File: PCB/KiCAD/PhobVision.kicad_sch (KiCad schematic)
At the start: 9 parts

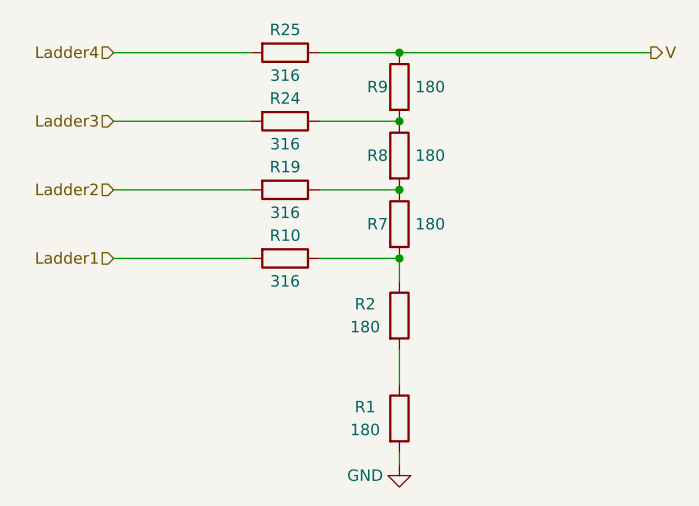
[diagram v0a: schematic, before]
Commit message: Assembly and fab upload
Upload schematic pdf and bom csv and ibom html docs
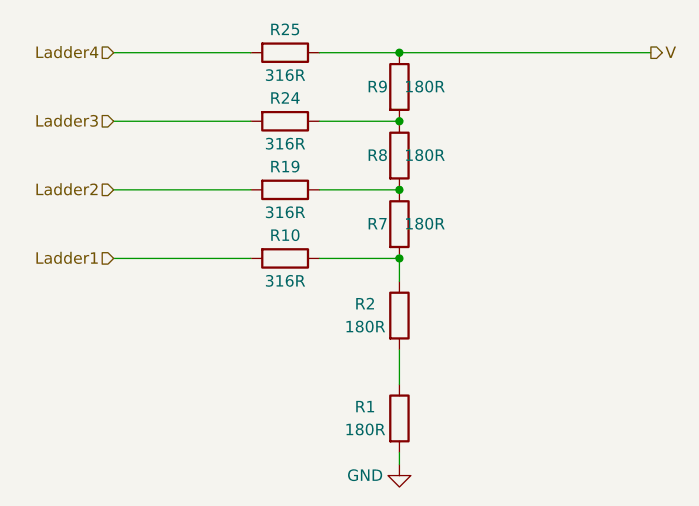
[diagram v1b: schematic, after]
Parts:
- R1, R2, R7, R8, R9: value 180 -> 180R; MPN (none) -> RC0402FR-07180RL; Manufacturer (none) -> YAGEO; Package (none) -> 0402; VARIANT (none) -> NoVar
- R10, R19, R24, R25: value 316 -> 316R; MPN (none) -> RC0402FR-07316RL; Manufacturer (none) -> YAGEO; Package (none) -> 0402; VARIANT (none) -> NoVar
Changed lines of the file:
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@@
       (effects (font (size 1.27 1.27)) (justify right))
     )
-    (property "Value" "180" (id 1) (at 144.78 87.63 0)
+    (property "Value" "180R" (id 1) (at 144.78 87.63 0)
       (effects (font (size 1.27 1.27)) (justify right))
     )
@@
     )
     (property "Datasheet" "~" (id 3) (at 139.7 87.63 0)
+      (effects (font (size 1.27 1.27)) hide)
+    )
+    (property "MPN" "RC0402FR-07180RL" (id 4) (at 139.7 87.63 0)
+      (effects (font (size 1.27 1.27)) hide)
+    )
+    (property "Manufacturer" "YAGEO" (id 5) (at 139.7 87.63 0)
+      (effects (font (size 1.27 1.27)) hide)
+    )
+    (property "Package" "0402" (id 6) (at 139.7 87.63 0)
+      (effects (font (size 1.27 1.27)) hide)
+    )
+    (property "VARIANT" "NoVar" (id 7) (at 139.7 87.63 0)
       (effects (font (size 1.27 1.27)) hide)
     )
@@
     (in_bom yes) (on_board yes)
     (property "Reference" "R19" (id 0) (at 127 88.9 90))
-    (property "Value" "316" (id 1) (at 127 93.98 90))
+    (property "Value" "316R" (id 1) (at 127 93.98 90))
     (property "Footprint" "PhobGCC_2_0_0_footprints:R_0402_1005Metric" (id 2) (at 127 89.662 90)
       (effects (font (size 1.27 1.27)) hide)
@@
       (effects (font (size 1.27 1.27)) hide)
     )
+    (property "MPN" "RC0402FR-07316RL" (id 4) (at 127 91.44 0)
+      (effects (font (size 1.27 1.27)) hide)
+    )
+    (property "Manufacturer" "YAGEO" (id 5) (at 127 91.44 0)
+      (effects (font (size 1.27 1.27)) hide)
+    )
+    (property "Package" "0402" (id 6) (at 127 91.44 0)
+      (effects (font (size 1.27 1.27)) hide)
+    )
+    (property "VARIANT" "NoVar" (id 7) (at 127 91.44 0)
+      (effects (font (size 1.27 1.27)) hide)
+    )
     (pin "1")
     (pin "2")
@@
     (in_bom yes) (on_board yes)
     (property "Reference" "R25" (id 0) (at 127 73.66 90))
-    (property "Value" "316" (id 1) (at 127 78.74 90))
+    (property "Value" "316R" (id 1) (at 127 78.74 90))
     (property "Footprint" "PhobGCC_2_0_0_footprints:R_0402_1005Metric" (id 2) (at 127 74.422 90)
       (effects (font (size 1.27 1.27)) hide)
@@
       (effects (font (size 1.27 1.27)) hide)
     )
+    (property "MPN" "RC0402FR-07316RL" (id 4) (at 127 76.2 0)
+      (effects (font (size 1.27 1.27)) hide)
+    )
+    (property "Manufacturer" "YAGEO" (id 5) (at 127 76.2 0)
+      (effects (font (size 1.27 1.27)) hide)
+    )
+    (property "Package" "0402" (id 6) (at 127 76.2 0)
+      (effects (font (size 1.27 1.27)) hide)
+    )
+    (property "VARIANT" "NoVar" (id 7) (at 127 76.2 0)
+      (effects (font (size 1.27 1.27)) hide)
+    )
     (pin "1")
     (pin "2")
@@
     (in_bom yes) (on_board yes)
     (property "Reference" "R10" (id 0) (at 127 96.52 90))
-    (property "Value" "316" (id 1) (at 127 101.6 90))
+    (property "Value" "316R" (id 1) (at 127 101.6 90))
     (property "Footprint" "PhobGCC_2_0_0_footprints:R_0402_1005Metric" (id 2) (at 127 97.282 90)
       (effects (font (size 1.27 1.27)) hide)
@@
       (effects (font (size 1.27 1.27)) hide)
     )
+    (property "MPN" "RC0402FR-07316RL" (id 4) (at 127 99.06 0)
+      (effects (font (size 1.27 1.27)) hide)
+    )
+    (property "Manufacturer" "YAGEO" (id 5) (at 127 99.06 0)
+      (effects (font (size 1.27 1.27)) hide)
+    )
+    (property "Package" "0402" (id 6) (at 127 99.06 0)
+      (effects (font (size 1.27 1.27)) hide)
+    )
+    (property "VARIANT" "NoVar" (id 7) (at 127 99.06 0)
+      (effects (font (size 1.27 1.27)) hide)
+    )
     (pin "1")
     (pin "2")
@@
       (effects (font (size 1.27 1.27)) (justify right))
     )
-    (property "Value" "180" (id 1) (at 144.78 95.25 0)
+    (property "Value" "180R" (id 1) (at 144.78 95.25 0)
       (effects (font (size 1.27 1.27)) (justify right))
     )
@@
       (effects (font (size 1.27 1.27)) hide)
     )
+    (property "MPN" "RC0402FR-07180RL" (id 4) (at 139.7 95.25 0)
+      (effects (font (size 1.27 1.27)) hide)
+    )
+    (property "Manufacturer" "YAGEO" (id 5) (at 139.7 95.25 0)
+      (effects (font (size 1.27 1.27)) hide)
+    )
+    (property "Package" "0402" (id 6) (at 139.7 95.25 0)
+      (effects (font (size 1.27 1.27)) hide)
+    )
+    (property "VARIANT" "NoVar" (id 7) (at 139.7 95.25 0)
+      (effects (font (size 1.27 1.27)) hide)
+    )
     (pin "1")
     (pin "2")
@@
     (in_bom yes) (on_board yes)
     (property "Reference" "R2" (id 0) (at 135.89 104.14 0))
-    (property "Value" "180" (id 1) (at 135.89 106.68 0))
+    (property "Value" "180R" (id 1) (at 135.89 106.68 0))
     (property "Footprint" "PhobGCC_2_0_0_footprints:R_0402_1005Metric" (id 2) (at 137.922 105.41 90)
       (effects (font (size 1.27 1.27)) hide)
@@
       (effects (font (size 1.27 1.27)) hide)
     )
+    (property "MPN" "RC0402FR-07180RL" (id 4) (at 139.7 105.41 0)
+      (effects (font (size 1.27 1.27)) hide)
+    )
+    (property "Manufacturer" "YAGEO" (id 5) (at 139.7 105.41 0)
+      (effects (font (size 1.27 1.27)) hide)
+    )
+    (property "Package" "0402" (id 6) (at 139.7 105.41 0)
+      (effects (font (size 1.27 1.27)) hide)
+    )
+    (property "VARIANT" "NoVar" (id 7) (at 139.7 105.41 0)
+      (effects (font (size 1.27 1.27)) hide)
+    )
     (pin "1")
     (pin "2")
@@
     (in_bom yes) (on_board yes)
     (property "Reference" "R1" (id 0) (at 135.89 115.57 0))
-    (property "Value" "180" (id 1) (at 135.89 118.11 0))
+    (property "Value" "180R" (id 1) (at 135.89 118.11 0))
     (property "Footprint" "PhobGCC_2_0_0_footprints:R_0402_1005Metric" (id 2) (at 137.922 116.84 90)
       (effects (font (size 1.27 1.27)) hide)
@@
       (effects (font (size 1.27 1.27)) hide)
     )
+    (property "MPN" "RC0402FR-07180RL" (id 4) (at 139.7 116.84 0)
+      (effects (font (size 1.27 1.27)) hide)
+    )
+    (property "Manufacturer" "YAGEO" (id 5) (at 139.7 116.84 0)
+      (effects (font (size 1.27 1.27)) hide)
+    )
+    (property "Package" "0402" (id 6) (at 139.7 116.84 0)
+      (effects (font (size 1.27 1.27)) hide)
+    )
+    (property "VARIANT" "NoVar" (id 7) (at 139.7 116.84 0)
+      (effects (font (size 1.27 1.27)) hide)
+    )
     (pin "1")
     (pin "2")
@@
       (effects (font (size 1.27 1.27)) (justify right))
     )
-    (property "Value" "180" (id 1) (at 144.78 80.01 0)
+    (property "Value" "180R" (id 1) (at 144.78 80.01 0)
       (effects (font (size 1.27 1.27)) (justify right))
     )
@@
       (effects (font (size 1.27 1.27)) hide)
     )
+    (property "MPN" "RC0402FR-07180RL" (id 4) (at 139.7 80.01 0)
+      (effects (font (size 1.27 1.27)) hide)
+    )
+    (property "Manufacturer" "YAGEO" (id 5) (at 139.7 80.01 0)
+      (effects (font (size 1.27 1.27)) hide)
+    )
+    (property "Package" "0402" (id 6) (at 139.7 80.01 0)
+      (effects (font (size 1.27 1.27)) hide)
+    )
+    (property "VARIANT" "NoVar" (id 7) (at 139.7 80.01 0)
+      (effects (font (size 1.27 1.27)) hide)
+    )
     (pin "1")
     (pin "2")
@@
     (in_bom yes) (on_board yes)
     (property "Reference" "R24" (id 0) (at 127 81.28 90))
-    (property "Value" "316" (id 1) (at 127 86.36 90))
+    (property "Value" "316R" (id 1) (at 127 86.36 90))
     (property "Footprint" "PhobGCC_2_0_0_footprints:R_0402_1005Metric" (id 2) (at 127 82.042 90)
       (effects (font (size 1.27 1.27)) hide)
@@
       (effects (font (size 1.27 1.27)) hide)
     )
+    (property "MPN" "RC0402FR-07316RL" (id 4) (at 127 83.82 0)
+      (effects (font (size 1.27 1.27)) hide)
+    )
+    (property "Manufacturer" "YAGEO" (id 5) (at 127 83.82 0)
+      (effects (font (size 1.27 1.27)) hide)
+    )
+    (property "Package" "0402" (id 6) (at 127 83.82 0)
+      (effects (font (size 1.27 1.27)) hide)
+    )
+    (property "VARIANT" "NoVar" (id 7) (at 127 83.82 0)
+      (effects (font (size 1.27 1.27)) hide)
+    )
